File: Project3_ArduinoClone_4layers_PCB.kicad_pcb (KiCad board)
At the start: 2 copper layers, 40.1 x 26.4 mm, 17 parts, among them J1 Serial, J2 Digital pins, J3 ICSP, J4 I2C, U1 24LC1025, U2 24LC1025, U3 DS1337_v1, U4 ATMEGA328P-AU, Y1 Crystal 32 MHz, Y2 Crystal 16 MHz

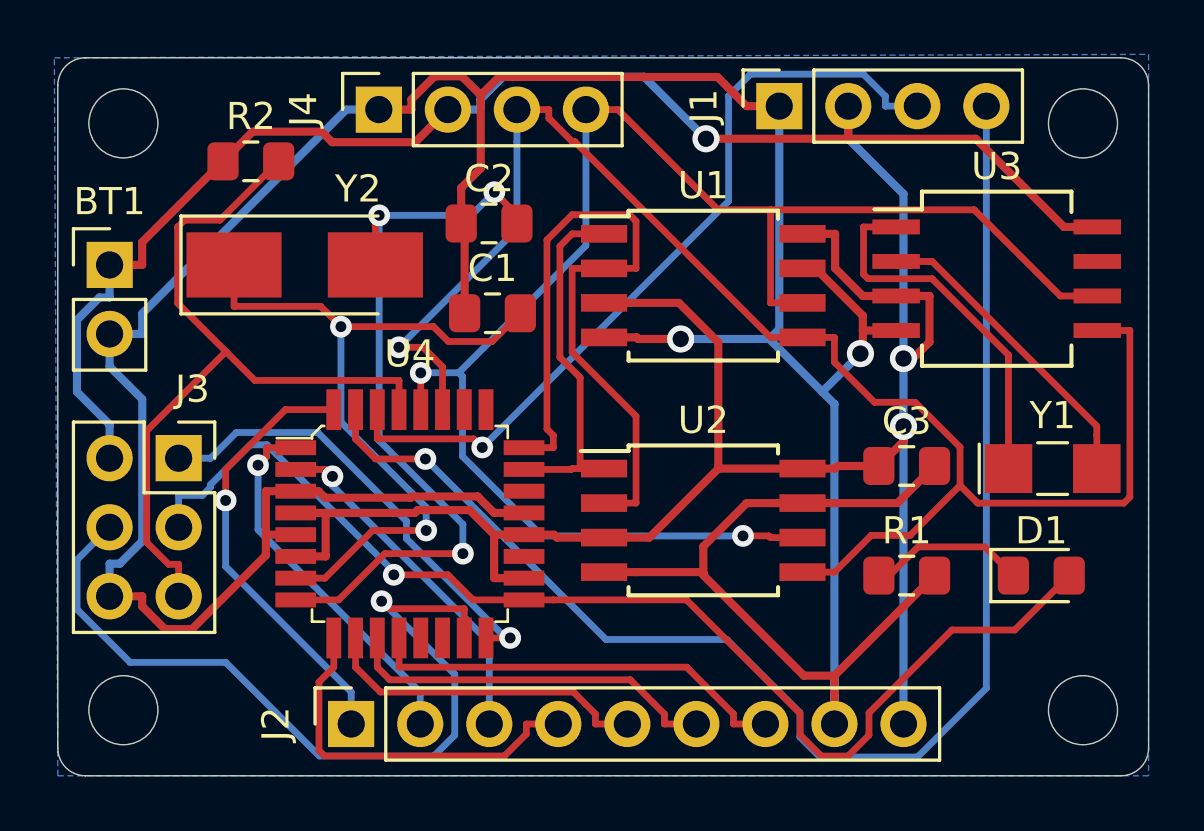
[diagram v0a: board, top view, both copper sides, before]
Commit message: Autoroute 2 and 4 layer version
Save different pcbnew files for each version
Create copper zone in 2 layer version,
and that is the main pcbnew file.
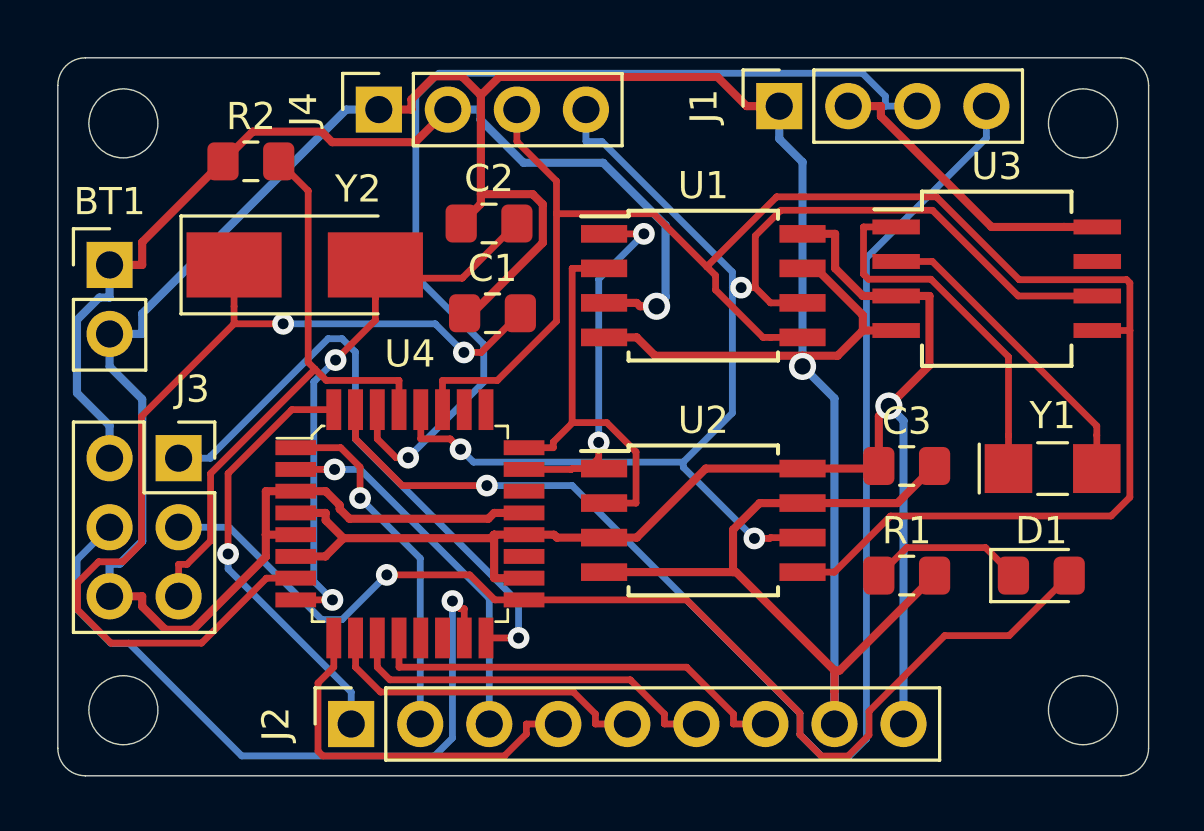
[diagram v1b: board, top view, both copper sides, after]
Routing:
- net /ADDS2: track 27.4 -> 15.0 mm
- net Net-(C1-Pad2): track 27.3 -> 36.7 mm
- net /RX: track 29.7 -> 37.5 mm
- net Net-(C2-Pad2): track 28.5 -> 20.9 mm, vias 3 -> 2
- net /SDA: track 58.7 -> 66.0 mm, vias 1 -> 0
- net /MISO: track 17.0 -> 22.8 mm
- net /RESET: track 28.8 -> 23.2 mm
- net /SCL: track 57.5 -> 52.1 mm, vias 2 -> 3
- net GND: track 135.7 -> 141.0 mm, vias 2 -> 1
- net /MOSI: track 30.2 -> 26.5 mm
- net /VCC: track 124.6 -> 122.2 mm, vias 3 -> 2
- net /SCK: track 43.3 -> 41.3 mm
- net /TX: track 52.1 -> 50.6 mm
- net /D3: track 13.8 -> 13.0 mm
- net /D4: track 13.0 -> 13.7 mm
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- removed copper zone on B.Cu, net GND
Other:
- copper layers 2 -> 4
